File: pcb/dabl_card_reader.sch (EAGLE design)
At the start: 2 parts, among them U1 TEENSY_3.1_WITH_AUDIO

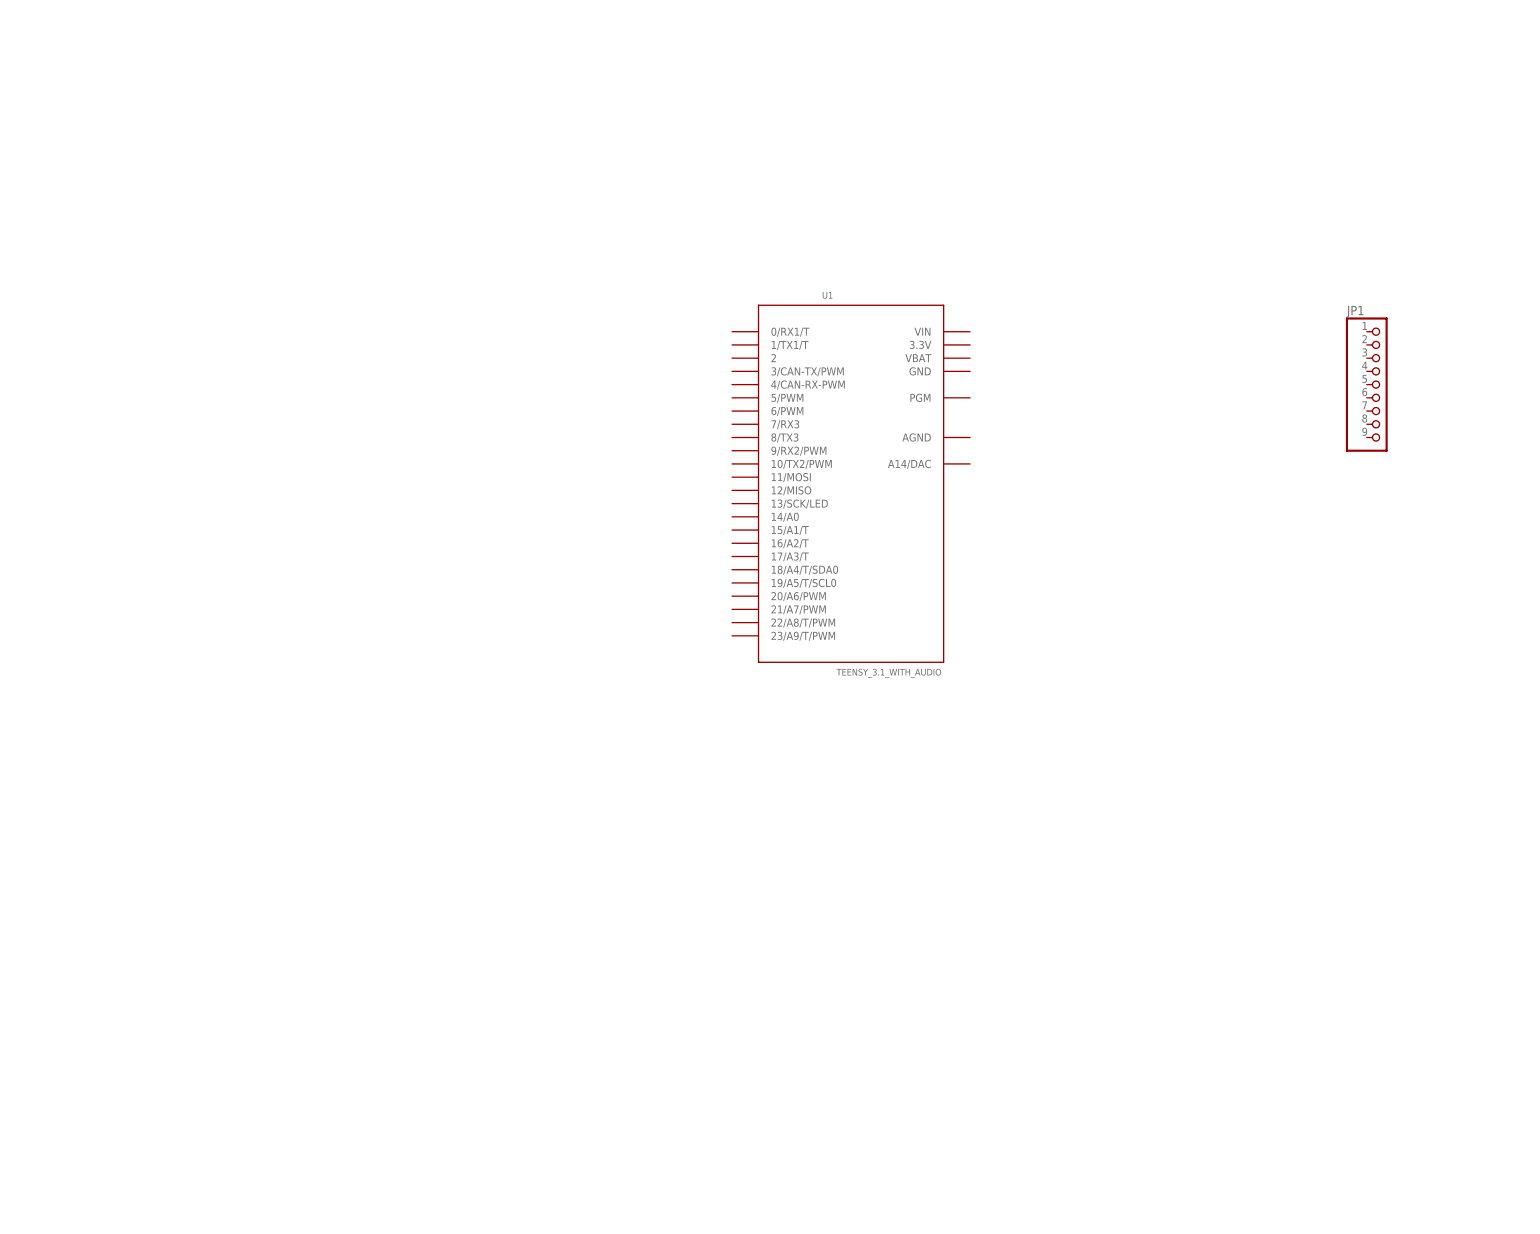
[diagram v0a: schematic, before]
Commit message: pulled in PN532 board dimensions and pin layout
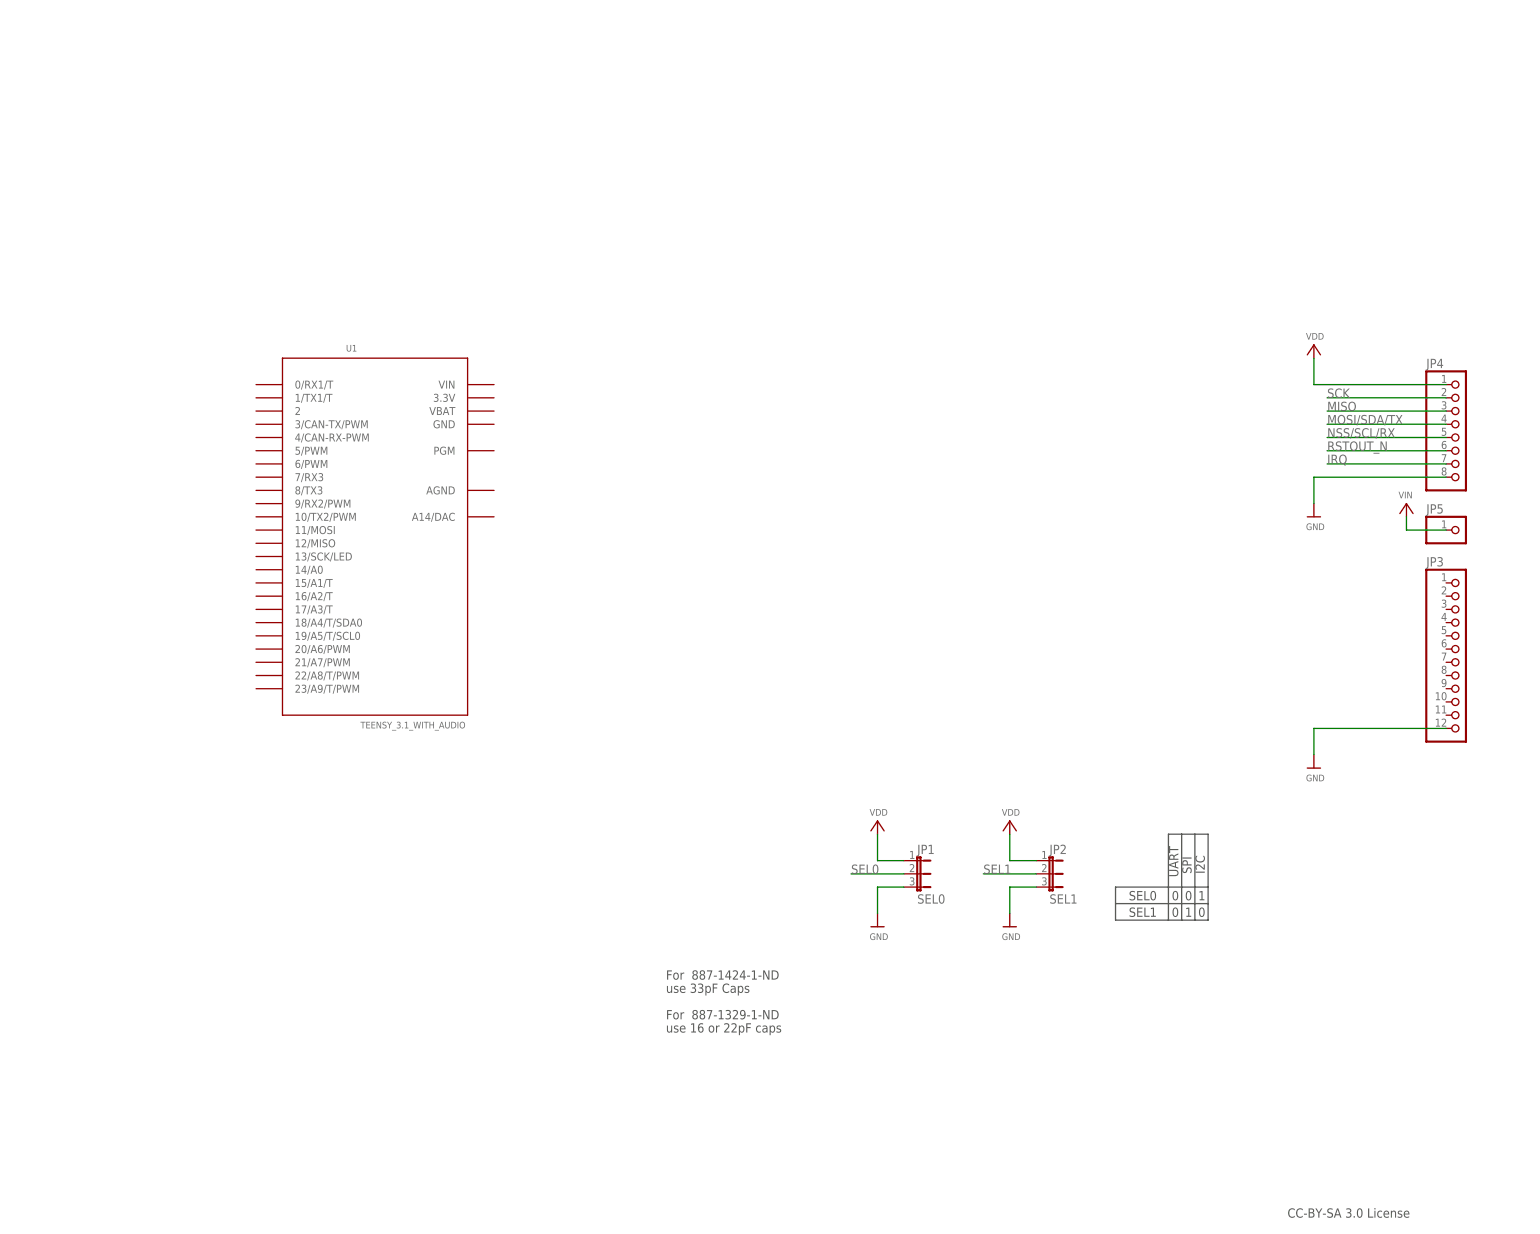
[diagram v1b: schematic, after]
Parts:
- added JP2: SEL1, microbuilder:JUMPER3
- added JP3: (no value), microbuilder:HEADER-1X12
- added JP4: (no value), microbuilder:HEADER-1X8ROUND
- added JP5: (no value), microbuilder:HEADER-1X1ROUND
- JP1: value (none) -> SEL0; device pinhead:PINHD-1X9 -> microbuilder:JUMPER3
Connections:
- new net GND: JP1.3, JP2.3, JP3.12, JP4.8
- new net IRQ: JP4.7
- new net MISO: JP4.3
- new net MOSI/SDA/TX: JP4.4
- new net NSS/SCL/RX: JP4.5
- new net RSTOUT_N: JP4.6
- new net SCK: JP4.2
- new net SEL0: JP1.2
- new net SEL1: JP2.2
- new net VDD: JP1.1, JP2.1, JP4.1
- new net VIN: JP5.1
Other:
- note added: "0"
- note added: "1"
- note added: "CC-BY-SA 3.0 License"
- note added: "For 887-1329-1-ND"
- note added: "For 887-1424-1-ND"
- note added: "I2C"
- note added: "SEL0"
- note added: "SEL1"
- note added: "SPI"
- note added: "UART"
- note added: "use 16 or 22pF caps"
- note added: "use 33pF Caps"
- moved on the sheet: U1

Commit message: full pcb for testing
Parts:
- added JP6: (no value), pinhead:PINHD-1X2
- added R1, R2, R3: 220, resistor:R-EU_0207/10
- JP3: device microbuilder:HEADER-1X12 -> pinhead:PINHD-1X4
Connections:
- removed net MOSI/SDA/TX: JP4.4
- removed net NSS/SCL/RX: JP4.5
- removed net SEL0: JP1.2
- removed net SEL1: JP2.2
- removed net VIN: JP5.1
- new net CS: JP4.5, U1.10/TX2/PWM
- new net MOSI: JP4.4, U1.11/MOSI
- new net N$1: JP3.4, R3.1
- new net N$10: R1.2, U1.14/A0
- new net N$2: JP3.3, R2.1
- new net N$5: JP3.1, R1.1
- new net N$8: R3.2, U1.16/A2/T
- new net N$9: R2.2, U1.15/A1/T
- net GND: now also JP1.2, JP3.2, JP6.2, U1.GND; no longer JP3.12
- net MISO: now also U1.12/MISO
- net SCK: now also U1.13/SCK/LED
- net VDD: now also JP2.2, U1.3.3V
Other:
- note removed: "CC-BY-SA 3.0 License"
- note removed: "For 887-1329-1-ND"
- note removed: "For 887-1424-1-ND"
- note removed: "use 16 or 22pF caps"
- note removed: "use 33pF Caps"

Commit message: finish initial pcb design
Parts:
- removed JP3: (no value), pinhead:PINHD-1X4
- added ESP8266: (no value), pinhead:PINHD-2X4
- added LED: (no value), pinhead:PINHD-1X4
- R1, R2, R3: device resistor:R-EU_0207/10 -> resistor:R-EU_M0805
- renumbered JP4 to SHIELD_PN532, JP6 to SHIELD_GND, U1 to TEENSY
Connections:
- removed net N$10: R1.2, TEENSY.14/A0
- removed net N$8: R3.2, TEENSY.16/A2/T
- removed net N$9: R2.2, TEENSY.15/A1/T
- removed net VDD: JP1.1, JP2.1, JP2.2, SHIELD_PN532.1, TEENSY.3.3V
- new net 3.3V: ESP8266.2, JP1.1, JP2.1, JP2.2, SHIELD_PN532.1, TEENSY.3.3V
- new net ESP_CHEN: ESP8266.6, TEENSY.6/PWM
- new net ESP_GPIO0: ESP8266.3, TEENSY.7/RX3
- new net ESP_GPIO2: ESP8266.5, TEENSY.8/TX3
- new net ESP_RST: ESP8266.4, TEENSY.2
- new net ESP_RX: ESP8266.1, TEENSY.1/TX1/T
- new net ESP_TX: ESP8266.8, TEENSY.0/RX1/T
- new net LED_B: R3.2, TEENSY.5/PWM
- new net LED_G: R2.2, TEENSY.4/CAN-RX-PWM
- new net LED_R: R1.2, TEENSY.3/CAN-TX/PWM
- net GND: now also ESP8266.7, LED.2; no longer JP3.2
- net N$1: now also LED.4; no longer JP3.4
- net N$2: now also LED.3; no longer JP3.3
- net N$5: now also LED.1; no longer JP3.1

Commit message: fix pcb traces
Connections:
- net 3.3V: now also ESP8266.8; no longer ESP8266.2
- net ESP_CHEN: now also ESP8266.4; no longer ESP8266.6
- net ESP_GPIO0: now also ESP8266.5; no longer ESP8266.3
- net ESP_GPIO2: now also ESP8266.3; no longer ESP8266.5
- net ESP_RST: now also ESP8266.6; no longer ESP8266.4
- net ESP_RX: now also ESP8266.7; no longer ESP8266.1
- net ESP_TX: now also ESP8266.2; no longer ESP8266.8
- net GND: now also ESP8266.1; no longer ESP8266.7
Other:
- moved on the sheet: ESP8266
